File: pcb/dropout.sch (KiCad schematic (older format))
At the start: 58 parts, among them SW1 Rotary_Encoder_Switch, SW2 SW_Push, U1 ProMicro, U2 ProMicro

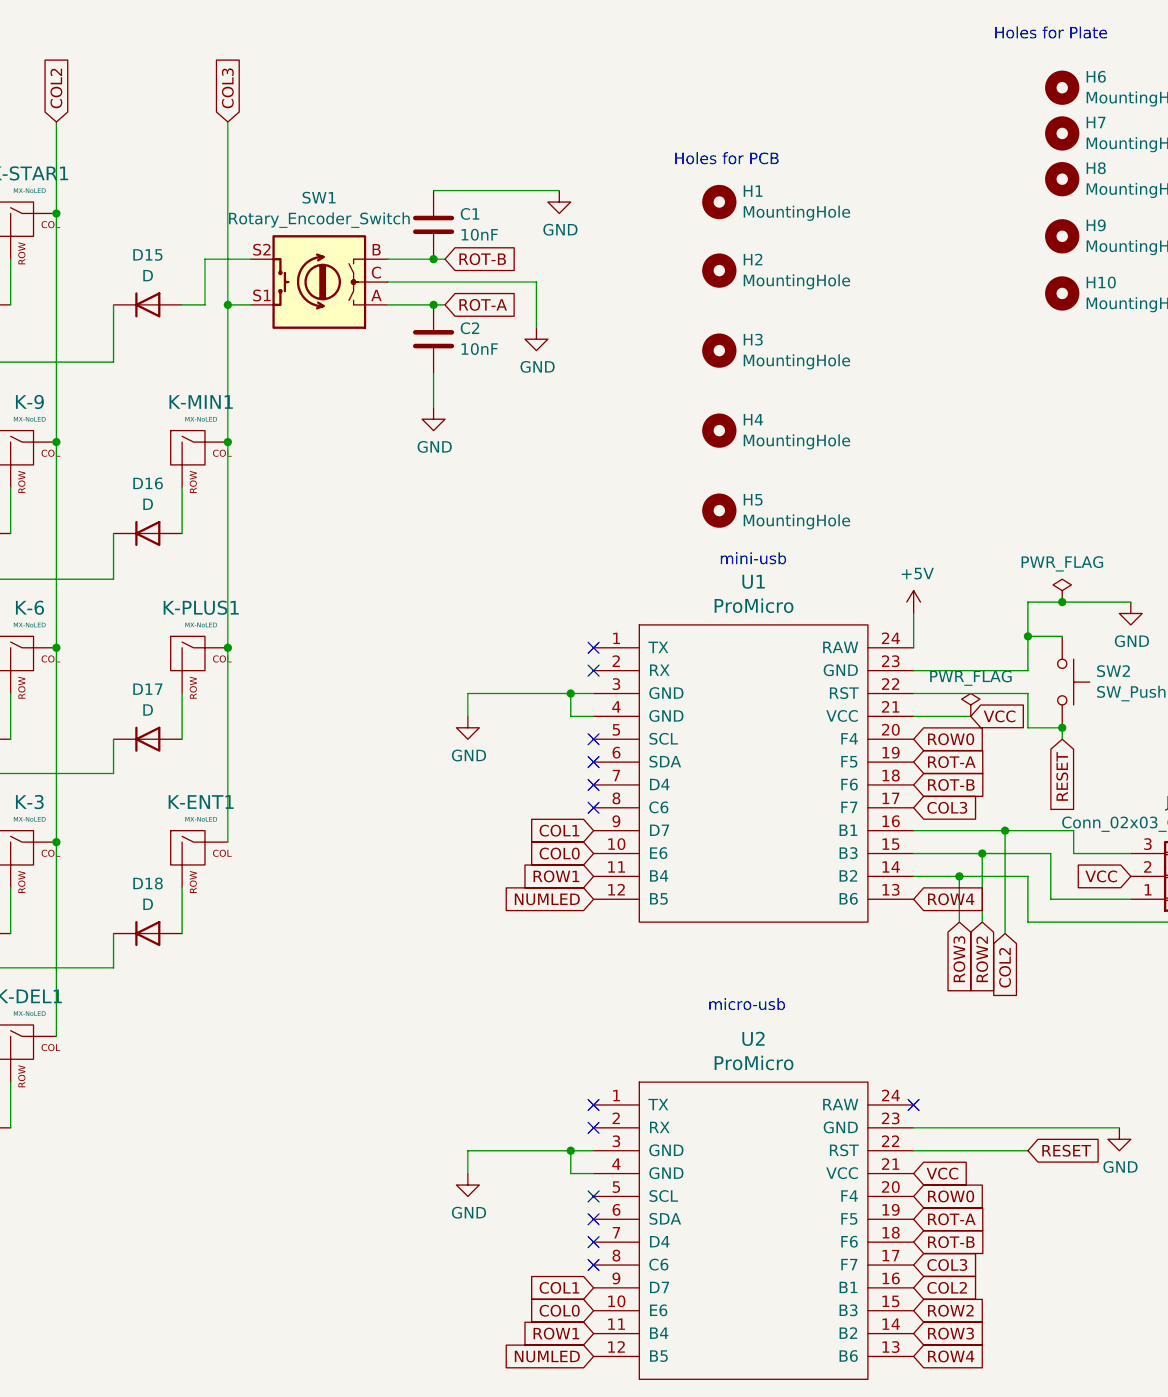
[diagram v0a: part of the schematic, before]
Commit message: alt-layout, replace encoder w/ switch
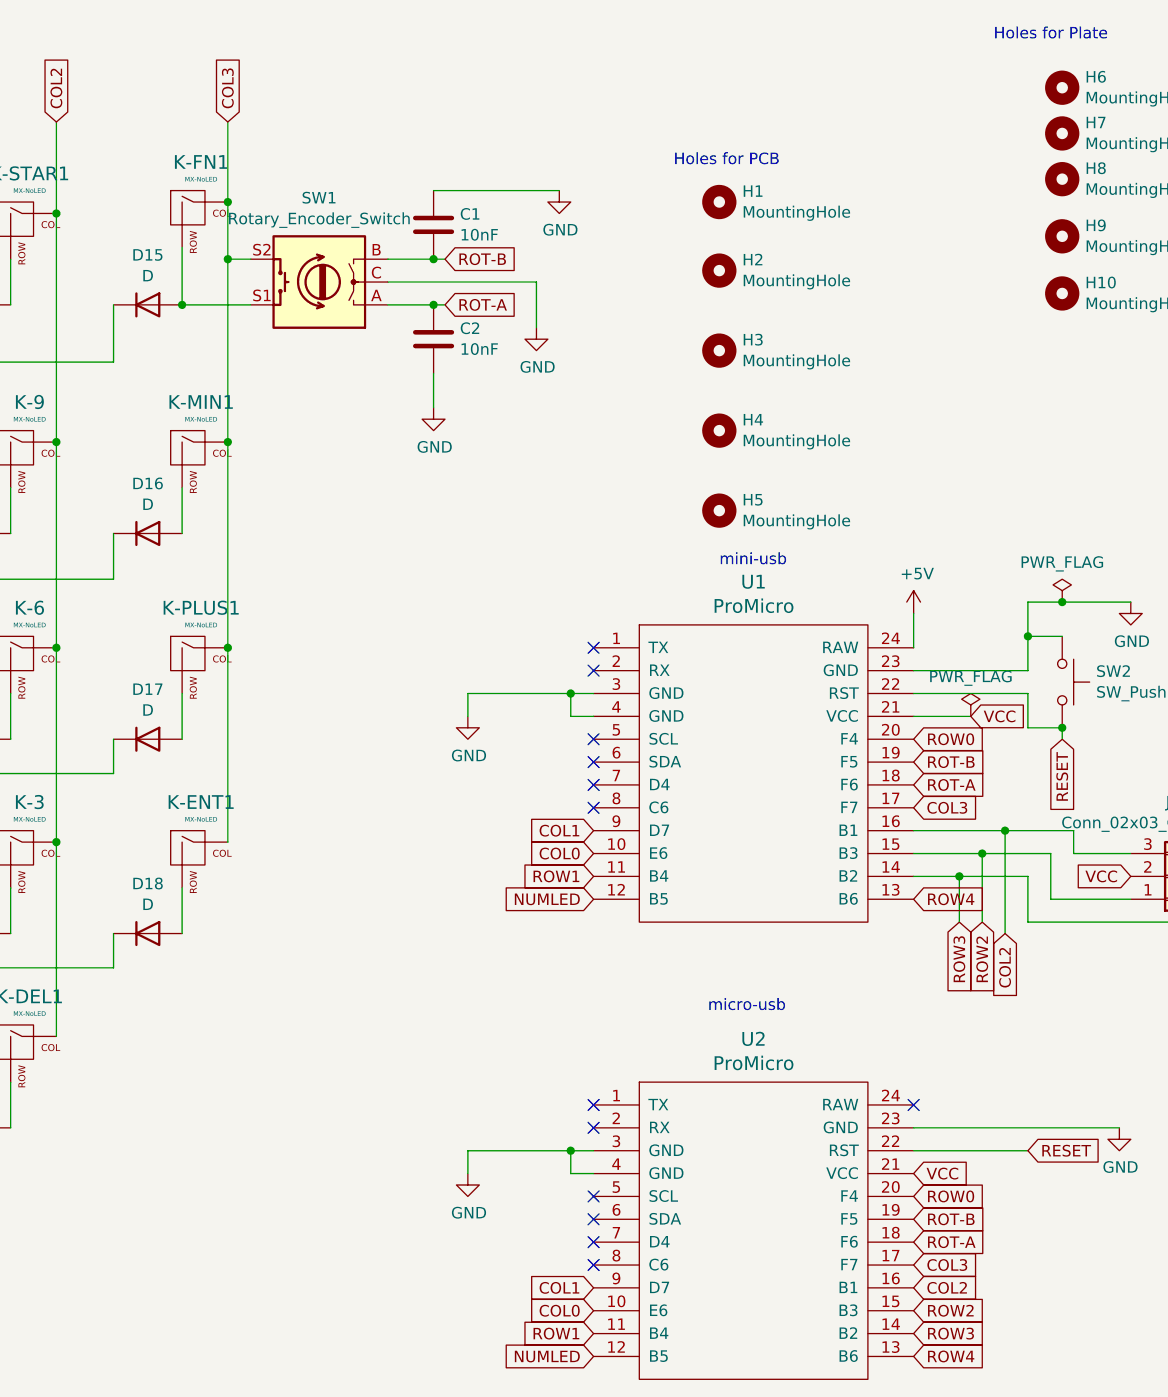
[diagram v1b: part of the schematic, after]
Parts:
- added K-FN1: MX-NoLED, MX_Only:MXOnly-1U-NoLED, symbol MX_Alps_Hybrid:MX-NoLED
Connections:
- net COL3: now also SW1.S2, K-FN1.1 (COL); no longer SW1.S1
- net ROT-A: now also U1.18 (F6), U2.18 (F6); no longer U1.19 (F5), U2.19 (F5)
- net ROT-B: now also U1.19 (F5), U2.19 (F5); no longer U1.18 (F6), U2.18 (F6)
- net at D15.2 (A): now also SW1.S1, K-FN1.2 (ROW); no longer SW1.S2
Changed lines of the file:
@@
 	1    0    0    -1
 $EndComp
-Text GLabel 8650 4400 2    50   Input ~ 0
-ROT-B
-Text GLabel 8650 4300 2    50   Input ~ 0
-ROT-A
 NoConn ~ 7250 4400
 $Comp
@@
 NoConn ~ 7250 4500
 Wire Wire Line
-	5650 1500 5650 2300
-Wire Wire Line
-	5450 2300 5550 2300
-Wire Wire Line
-	5550 2300 5550 2100
-Wire Wire Line
-	5550 2100 5750 2100
-Wire Wire Line
-	5750 2300 5650 2300
-Connection ~ 5650 2300
-Wire Wire Line
-	5650 2300 5650 2900
+	5650 1500 5650 1850
 NoConn ~ 7250 4200
 $Comp
@@
 Text GLabel 8650 6500 2    50   Input ~ 0
 COL3
-Text GLabel 8650 6400 2    50   Input ~ 0
-ROT-B
-Text GLabel 8650 6300 2    50   Input ~ 0
-ROT-A
 Wire Wire Line
 	8650 6000 9150 6000
@@
 	8650 3800 8650 3650
 $Comp
-L power:GND #PWR?
+L power:GND #PWR0107
 U 1 1 5FF1CEC0
 P 3000 2300
-F 0 "#PWR?" H 3000 2050 50  0001 C CNN
+F 0 "#PWR0107" H 3000 2050 50  0001 C CNN
 F 1 "GND" H 3005 2127 50  0000 C CNN
 F 2 "" H 3000 2300 50  0001 C CNN
@@
 	1    0    0    -1
 $EndComp
+$Comp
+L MX_Alps_Hybrid:MX-NoLED K-FN1
+U 1 1 5FD59D56
+P 5500 1900
+F 0 "K-FN1" H 5533 2123 60  0000 C CNN
+F 1 "MX-NoLED" H 5533 2049 20  0000 C CNN
+F 2 "MX_Only:MXOnly-1U-NoLED" H 4875 1875 60  0001 C CNN
+F 3 "" H 4875 1875 60  0001 C CNN
+	1    5500 1900
+	1    0    0    -1
+$EndComp
+Connection ~ 5650 1850
+Text GLabel 8650 6300 2    50   Input ~ 0
+ROT-B
+Text GLabel 8650 6400 2    50   Input ~ 0
+ROT-A
+Text GLabel 8650 4300 2    50   Input ~ 0
+ROT-B
+Text GLabel 8650 4400 2    50   Input ~ 0
+ROT-A
+Wire Wire Line
+	5650 1850 5650 2100
+Wire Wire Line
+	5450 2050 5450 2300
+Wire Wire Line
+	5450 2300 5750 2300
+Connection ~ 5450 2300
+Wire Wire Line
+	5650 2100 5750 2100
+Connection ~ 5650 2100
+Wire Wire Line
+	5650 2100 5650 2900
 $EndSCHEMATC

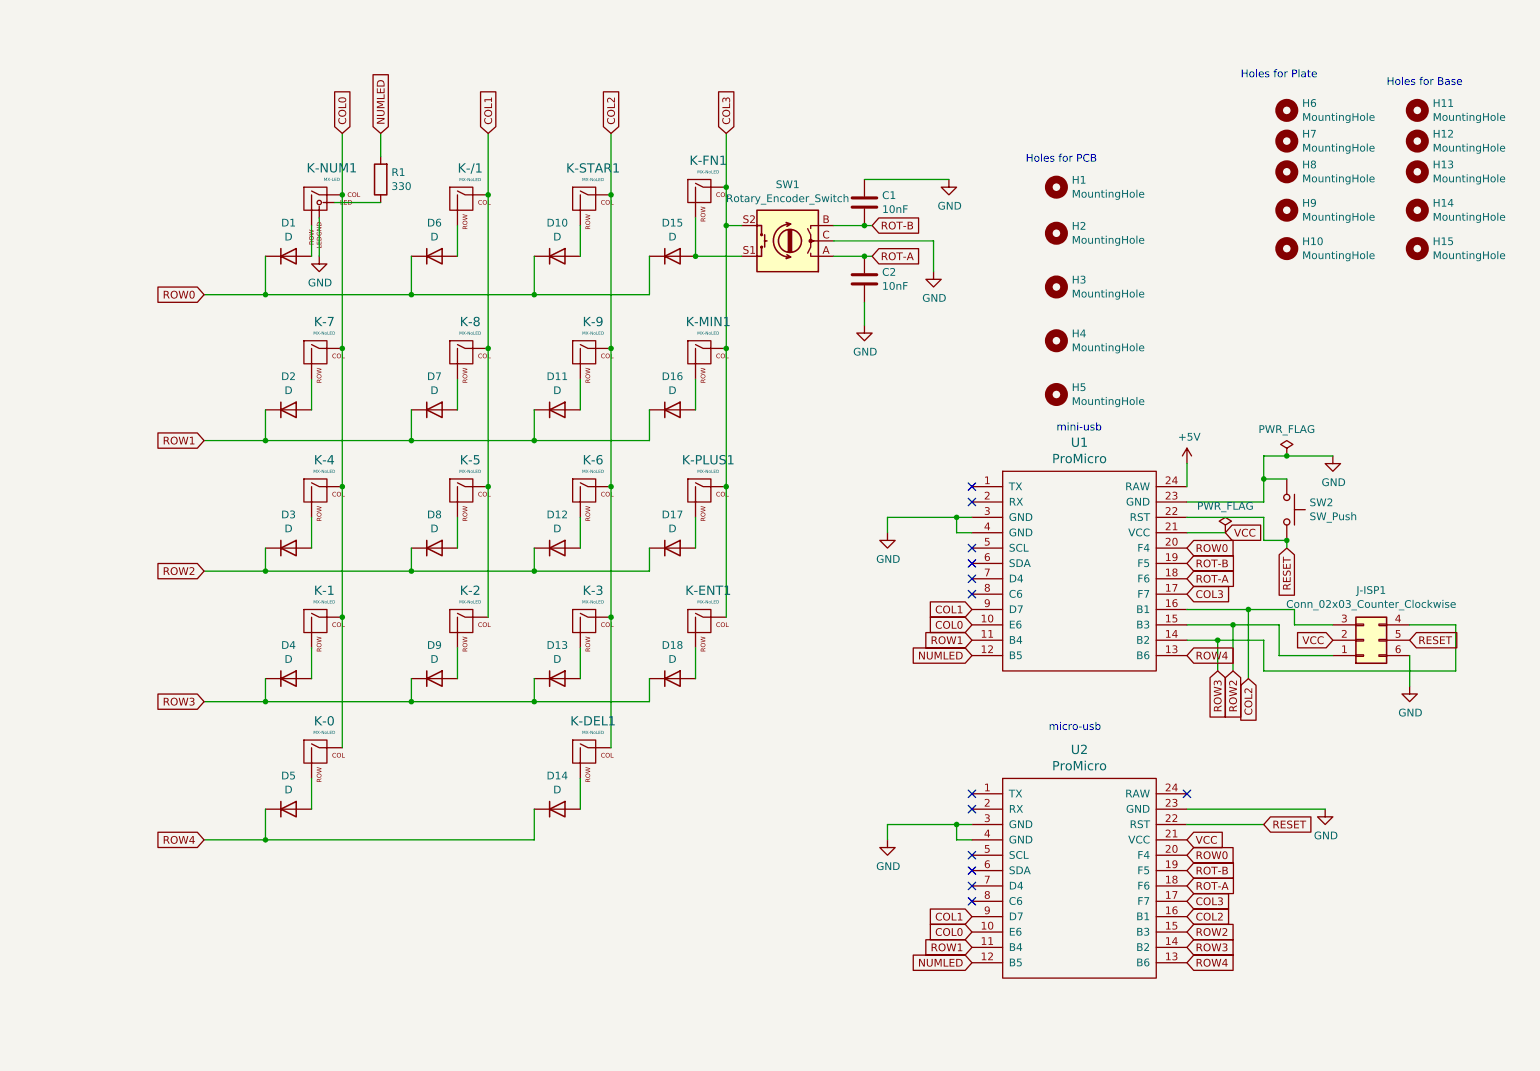
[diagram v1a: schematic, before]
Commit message: 5v -> led -> pin (numlock led)
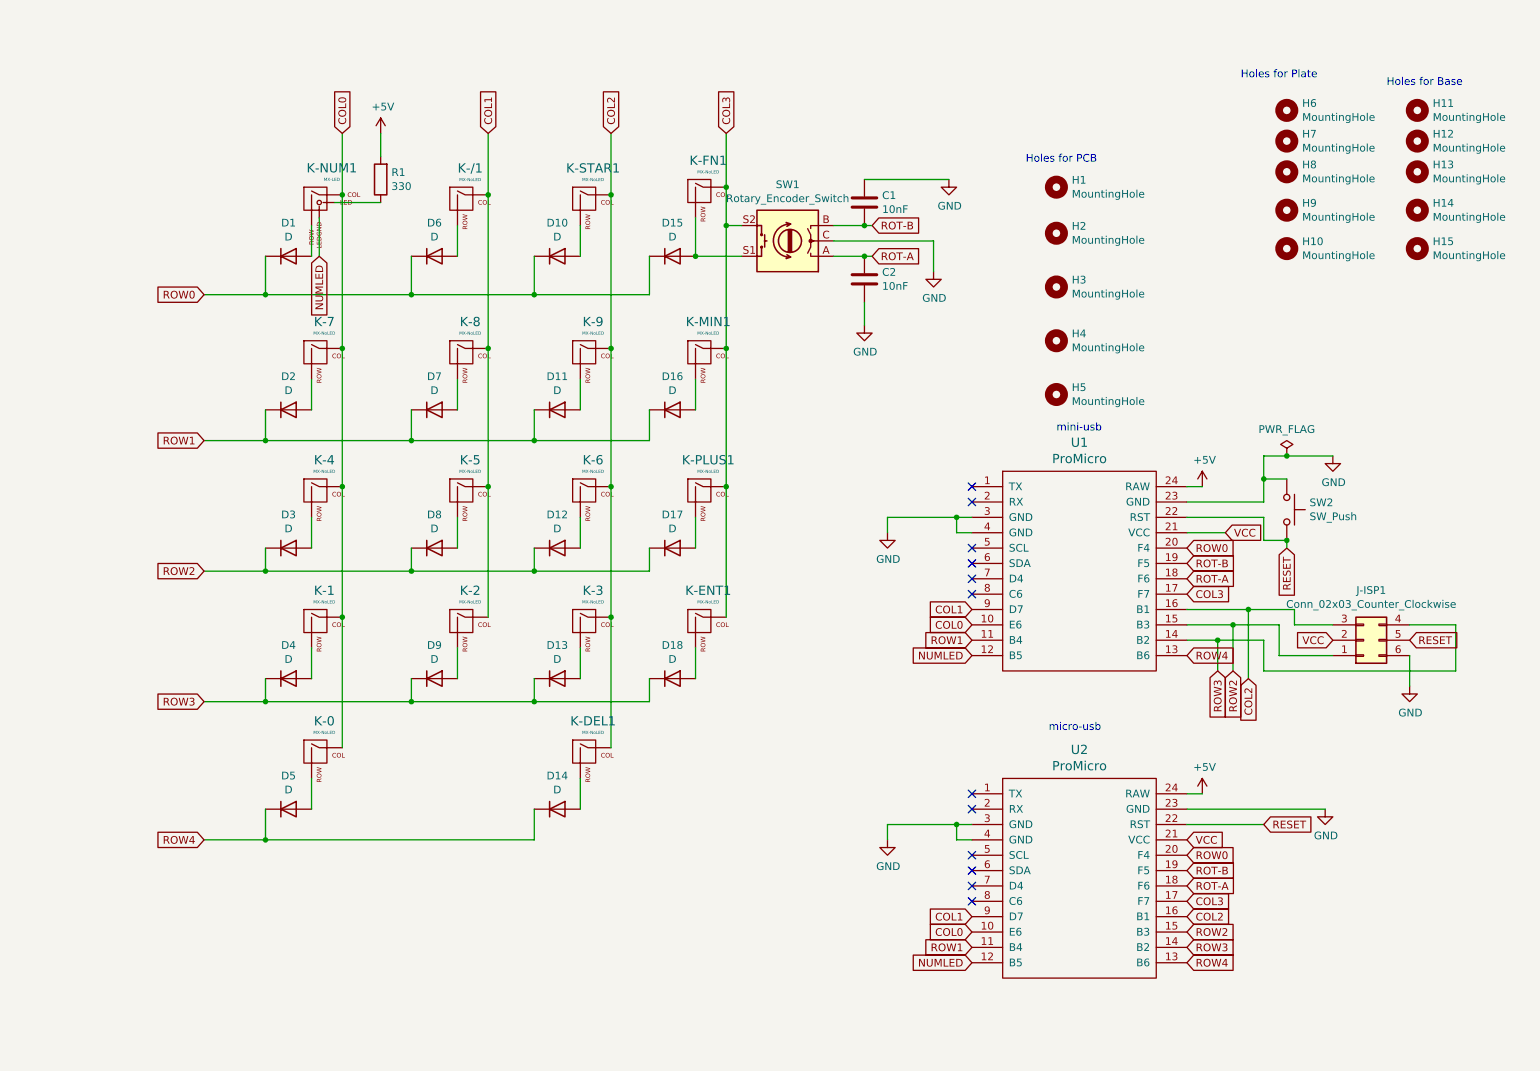
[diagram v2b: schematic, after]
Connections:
- net +5V: now also R1.2, U2.24 (RAW)
- net GND: no longer K-NUM1.4 (LEDGND)
- net NUMLED: now also K-NUM1.4 (LEDGND); no longer R1.2
- no-connect marks 13 -> 12
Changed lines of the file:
@@
 Wire Wire Line
 	3100 1950 3400 1950
-Wire Wire Line
-	3400 1650 3400 1500
-Text GLabel 3400 1500 1    50   Input ~ 0
+Text GLabel 3000 2300 3    50   Input ~ 0
 NUMLED
 $Comp
@@
 Wire Wire Line
 	6700 6100 6700 6000
-NoConn ~ 8650 5800
 Text GLabel 8650 6100 2    50   Input ~ 0
 VCC
@@
 Wire Wire Line
 	8650 5900 9550 5900
-$Comp
-L promicro:ProMicro U2
-U 1 1 5FD6075C
-P 7950 6550
-F 0 "U2" H 7950 7587 60  0000 C CNN
-F 1 "ProMicro" H 7950 7481 60  0000 C CNN
-F 2 "promicro:ProMicro" H 8050 5500 60  0001 C CNN
-F 3 "" H 8050 5500 60  0000 C CNN
-	1    7950 6550
-	1    0    0    -1
-$EndComp
 NoConn ~ 7250 6200
 NoConn ~ 7250 6500
@@
 Text GLabel 7250 6800 0    50   Input ~ 0
 ROW1
-$Comp
-L power:PWR_FLAG #FLG0102
-U 1 1 5FF0027E
-P 8900 4100
-F 0 "#FLG0102" H 8900 4175 50  0001 C CNN
-F 1 "PWR_FLAG" H 8900 4273 50  0000 C CNN
-F 2 "" H 8900 4100 50  0001 C CNN
-F 3 "~" H 8900 4100 50  0001 C CNN
-	1    8900 4100
-	1    0    0    -1
-$EndComp
 Wire Wire Line
 	8650 4100 8900 4100
-$Comp
-L power:+5V #PWR0106
-U 1 1 5FF0E2E0
-P 8650 3650
-F 0 "#PWR0106" H 8650 3500 50  0001 C CNN
-F 1 "+5V" H 8665 3823 50  0000 C CNN
-F 2 "" H 8650 3650 50  0001 C CNN
-F 3 "" H 8650 3650 50  0001 C CNN
-	1    8650 3650
-	1    0    0    -1
-$EndComp
-Wire Wire Line
-	8650 3800 8650 3650
-$Comp
-L power:GND #PWR0107
-U 1 1 5FF1CEC0
-P 3000 2300
-F 0 "#PWR0107" H 3000 2050 50  0001 C CNN
-F 1 "GND" H 3005 2127 50  0000 C CNN
-F 2 "" H 3000 2300 50  0001 C CNN
-F 3 "" H 3000 2300 50  0001 C CNN
-	1    3000 2300
-	1    0    0    -1
-$EndComp
 $Comp
 L MX_Alps_Hybrid:MX-NoLED K-FN1
@@
 Wire Wire Line
 	5650 2100 5650 2900
+$Comp
+L power:+5V #PWR0106
+U 1 1 5FD6C1AA
+P 8750 3800
+F 0 "#PWR0106" H 8750 3650 50  0001 C CNN
+F 1 "+5V" H 8765 3973 50  0000 C CNN
+F 2 "" H 8750 3800 50  0001 C CNN
+F 3 "" H 8750 3800 50  0001 C CNN
+	1    8750 3800
+	1    0    0    -1
+$EndComp
+$Comp
+L promicro:ProMicro U2
+U 1 1 5FD6075C
+P 7950 6550
+F 0 "U2" H 7950 7587 60  0000 C CNN
+F 1 "ProMicro" H 7950 7481 60  0000 C CNN
+F 2 "promicro:ProMicro" H 8050 5500 60  0001 C CNN
+F 3 "" H 8050 5500 60  0000 C CNN
+	1    7950 6550
+	1    0    0    -1
+$EndComp
+$Comp
+L power:+5V #PWR0107
+U 1 1 5FD7658D
+P 8750 5800
+F 0 "#PWR0107" H 8750 5650 50  0001 C CNN
+F 1 "+5V" H 8765 5973 50  0000 C CNN
+F 2 "" H 8750 5800 50  0001 C CNN
+F 3 "" H 8750 5800 50  0001 C CNN
+	1    8750 5800
+	1    0    0    -1
+$EndComp
+Wire Wire Line
+	8650 5800 8750 5800
+$Comp
+L power:+5V #PWR0108
+U 1 1 5FD7B580
+P 3400 1500
+F 0 "#PWR0108" H 3400 1350 50  0001 C CNN
+F 1 "+5V" H 3415 1673 50  0000 C CNN
+F 2 "" H 3400 1500 50  0001 C CNN
+F 3 "" H 3400 1500 50  0001 C CNN
+	1    3400 1500
+	1    0    0    -1
+$EndComp
+Wire Wire Line
+	3400 1500 3400 1650
+Wire Wire Line
+	8650 3800 8750 3800
 $EndSCHEMATC
